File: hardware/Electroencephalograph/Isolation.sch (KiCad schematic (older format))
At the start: 21 parts, among them U4 THI3-0511, U5 ADUM2401BRWZ

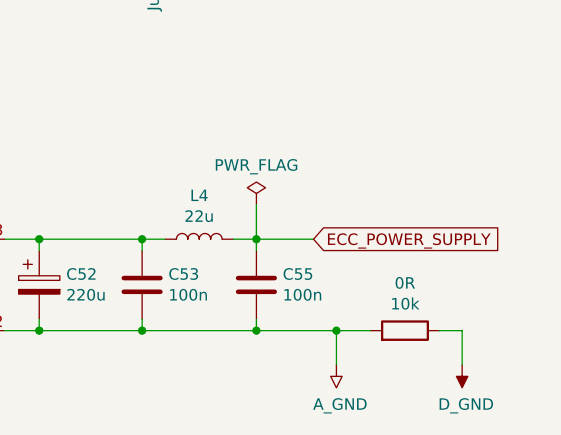
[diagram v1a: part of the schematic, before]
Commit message: add support for esp module
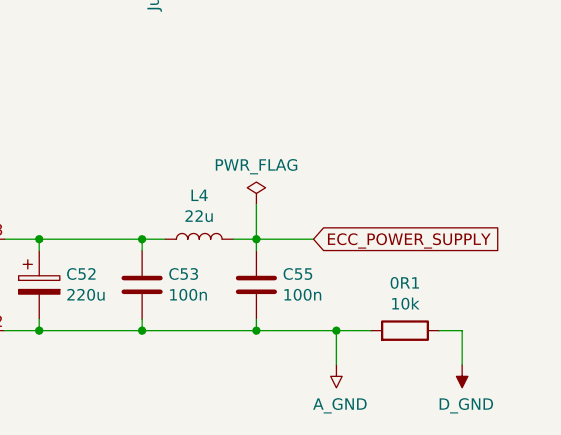
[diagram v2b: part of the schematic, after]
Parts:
- renumbered 0R to 0R1
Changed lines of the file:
@@
 AR Path="/5DD5C7F6/5EC9AC63" Ref="R?"  Part="1"
 AR Path="/5E142744/5EC9AC63" Ref="R?"  Part="1"
-AR Path="/5DFE0AD6/5EC9AC63" Ref="0R"  Part="1"
-F 0 "0R" V 5557 5200 50  0000 C CNN
+AR Path="/5DFE0AD6/5EC9AC63" Ref="0R1"  Part="1"
+F 0 "0R1" V 5557 5200 50  0000 C CNN
 F 1 "10k" V 5466 5200 50  0000 C CNN
 F 2 "Resistor_SMD:R_0402_1005Metric" V 5280 5200 50  0001 C CNN
